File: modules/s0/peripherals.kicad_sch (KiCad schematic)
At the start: 35 parts, among them J2 Conn_Coaxial, J3 Conn_Coaxial, Q1 SS8050, Q2 SS8050, Q3 SS8050, U2 SIM7080G, U3 TXB0108RGY, U8 NANO SIM XG6P H1.35

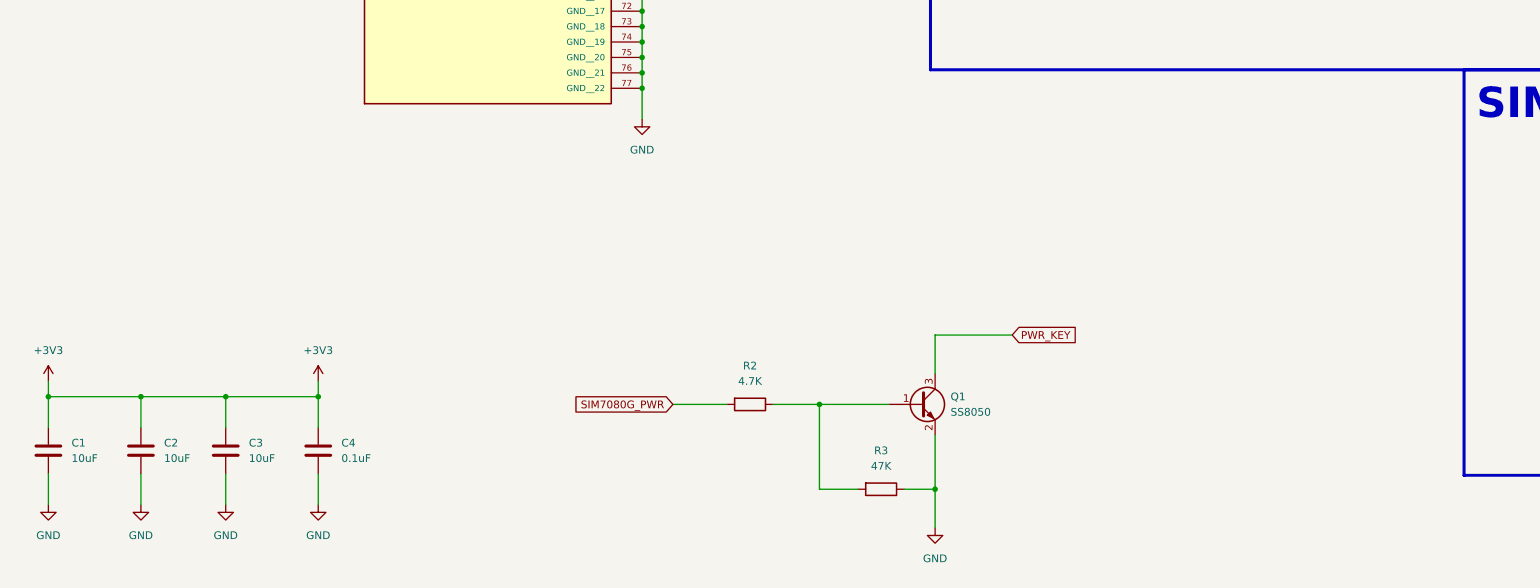
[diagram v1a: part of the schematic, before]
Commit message: chore:Modify BOM in production
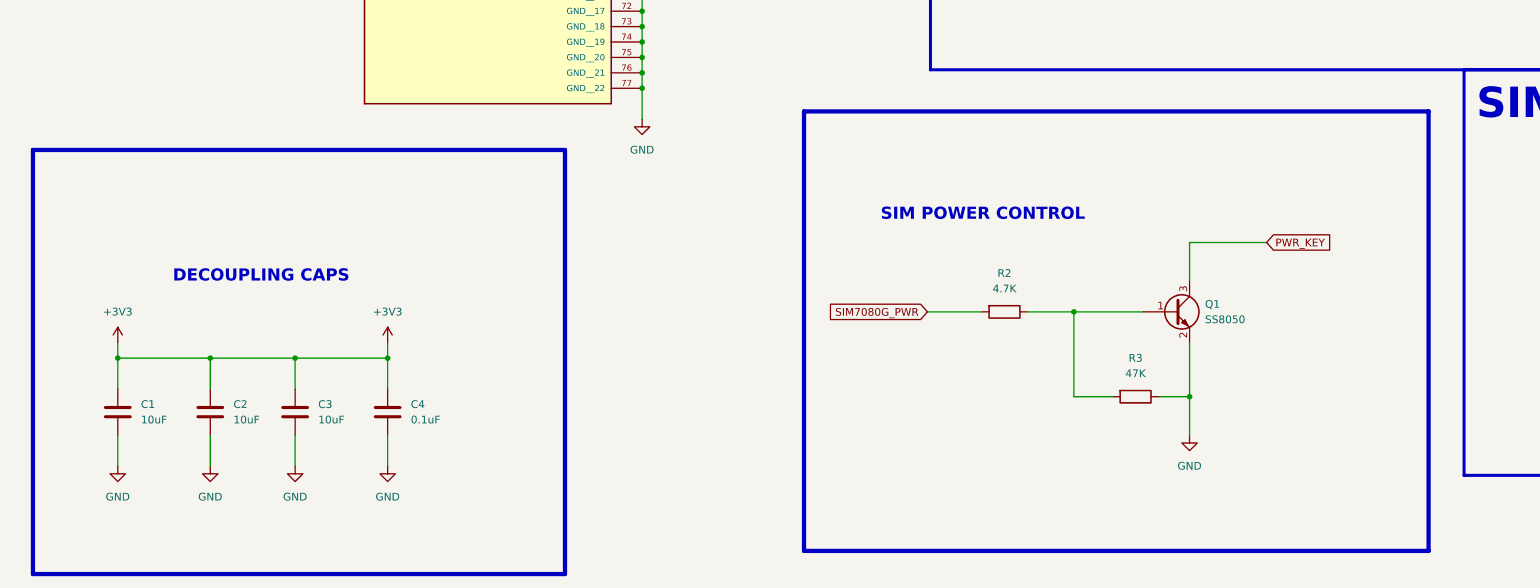
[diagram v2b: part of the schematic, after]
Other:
- note added: "DECOUPLING CAPS"
- note added: "SIM POWER CONTROL"
- moved on the sheet: C1, C2, C3, C4, Q1, R2, R3

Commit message: Modified Schematics and BOM
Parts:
- added D5: ESD9B5.0ST5G, Diode_SMD:D_SOD-923, symbol Diode:ESD9B5.0ST5G
- U5: renamed from U8; JLCPCB (none) -> C77877; LCSC Part C7529386 -> (none)
- renumbered C7 to C10, C9 to C11, C10 to C12, C1 to C3, C2 to C4, C3 to C5, C4 to C6, C5 to C7, C6 to C8, C8 to C9, D3 to D2, D1 to D3, D2 to D4, J2 to J5, J3 to J6, L1 to L2, L2 to L3, Q3 to Q2, Q2 to Q3, R9 to R10, R1 to R3, R2 to R4, R6 to R5, R4 to R6, R3 to R7, R5 to R8, R7 to R9, U3 to U1, U2 to U3
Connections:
- net GND: now also D5.1 (A1)
- net PWR_KEY: now also D5.2 (A2)

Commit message: chore: route the board with changes
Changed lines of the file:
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@@
+	)
+	(rectangle
+		(start 17.78 212.09)
+		(end 123.19 278.13)
+		(stroke
+			(width 0.5)
+			(type default)
+			(color 132 0 132 1)
+		)
+		(fill
+			(type none)
+		)
 	)
 	(rectangle
@@
 	)
 	(rectangle
-		(start 158.75 193.04)
-		(end 261.62 265.43)
+		(start 179.578 11.938)
+		(end 286.258 186.182)
 		(stroke
-			(width 0.7)
+			(width 0.5)
 			(type default)
+			(color 132 0 132 1)
 		)
 		(fill
@@
 	)
 	(rectangle
-		(start 31.75 199.39)
-		(end 119.38 269.24)
-		(stroke
-			(width 0.7)
-			(type default)
-		)
-		(fill
-			(type none)
-		)
-	)
-	(rectangle
-		(start 179.578 11.938)
-		(end 286.258 186.182)
+		(start 157.48 201.93)
+		(end 262.89 267.97)
 		(stroke
 			(width 0.5)
